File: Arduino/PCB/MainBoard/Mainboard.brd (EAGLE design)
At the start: 94.9 x 80 mm, 58 parts, among them IC1 ULN2803ADW, IC2 DS1338Z-33+, J1 FTDI_DEVICE, J2 FTDI_DEVICE, J3 DC-005, U1 ATMEGA328-AU, U4 R-78B5.0-2.0, X1 16Mhz, X2 32.768kHz

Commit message: Mainboard
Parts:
- removed U$1, U$2, U$3, U$4, U$5, U$6, U$7, U$8: GF1A-E3/67A, MainboardComponents:DO-214BA
- removed X2: 32.768kHz, IQD-Frequency-Products:HC49-3L
- added DF1, DF2, DF3, DF4, DF5, DF6, DF7, DF8: GF1A-E3/67A, MainboardComponents:DO-214BA
- added J4: XBEE CONN, SparkFun-Connectors:FTDI_DEVICE_SIDE
- added JP3: (no value), jumper:JP2
- added Q1: 32.768kHz, MainboardComponents:CRYSAL_RADIA_6.2MM
- J1: value FTDI_DEVICE -> ARDUINO PROG
- J2: value FTDI_DEVICE -> BOOTL PROG
- R1, R10, R4, R5, R6, R7, R8, R9: value 580 -> 5k3
- moved U4 3.09 mm to (7.11, 37.3)
- moved C1 2.54 mm to (68.6, 54.6)
- moved L1 2.05 mm to (11.7, 23.6)
- moved C4 2.05 mm to (14.2, 17.3), flipped to the top, turned to 0 degrees
- moved C5 2.04 mm to (14.1, 30.0), flipped to the top, turned to 0 degrees
- moved J3 1.08 mm to (9.65, 10.9)
- moved R2 0.90 mm to (60.3, 56.5)
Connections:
- new net N$41: IC2.1, Q1.P$2
- new net N$42: J4.P$5, XB1.16
- net +12V: now also DF1.C, DF2.C, DF3.C, DF4.C, DF5.C, DF6.C, DF7.C, DF8.C, IC1.10; no longer U$1.C, U$2.C, U$3.C, U$4.C, U$5.C, U$6.C, U$7.C, U$8.C
- net +3V3: now also J4.P$4
- net GND: now also J4.P$6, JP3.1, XB1.9; no longer IC1.10
- net N$13: now also J4.P$1, XB1.12; no longer IC2.1, X2.1
- net N$14: now also Q1.P$1; no longer X2.3
- net N$2: now also JP3.2
- net N$3: now also J4.P$2
- net N$35: now also J4.P$3
- net R0: now also DF8.A; no longer U$8.A
- net R1: now also DF7.A; no longer U$7.A
- net R2: now also DF6.A; no longer U$6.A
- net R3: now also DF5.A; no longer U$5.A
- net R4: now also DF4.A; no longer U$4.A
- net R5: now also DF3.A; no longer U$3.A
- net R6: now also DF2.A; no longer U$2.A
- net R7: now also DF1.A; no longer U$1.A
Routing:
- net GND: track 221.1 -> 258.6 mm
- net +3V3: track 131.4 -> 162.9 mm
- net N$35: track 38.2 -> 68.2 mm
- net N$13: track 6.39 -> 35.9 mm
- net N$2: track 48.7 -> 74.9 mm
- net N$42: track 0.00 -> 23.7 mm
- net N$3: track 38.0 -> 60.3 mm
- net N$23: track 88.9 -> 106.0 mm, vias 1 -> 0
- net N$24: track 92.5 -> 81.7 mm
- net +12V: track 157.6 -> 163.5 mm, vias 0 -> 1
- net +5V: track 65.7 -> 61.6 mm
- net N$41: track 0.00 -> 4.06 mm
- net N$7: track 13.4 -> 10.4 mm
- net N$20: track 36.2 -> 33.5 mm
- net N$6: track 13.0 -> 10.8 mm
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
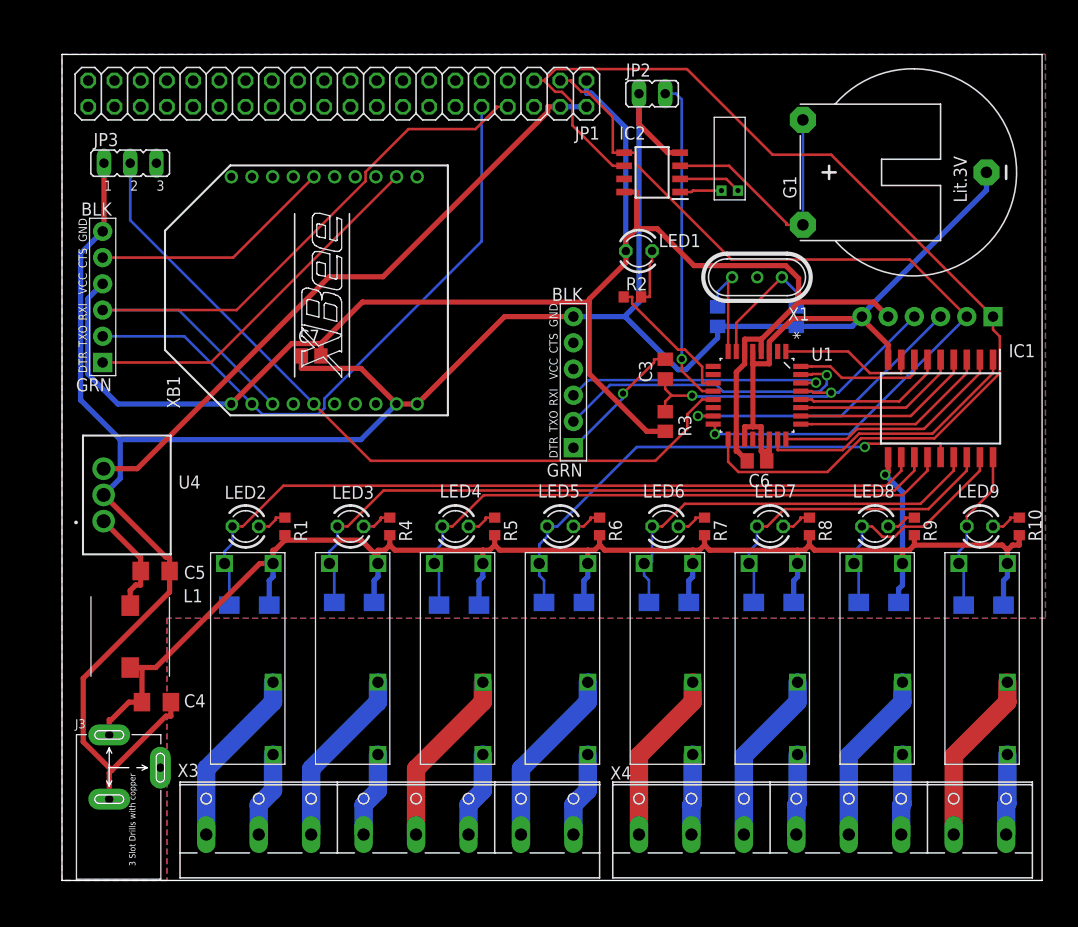
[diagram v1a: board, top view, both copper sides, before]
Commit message: 
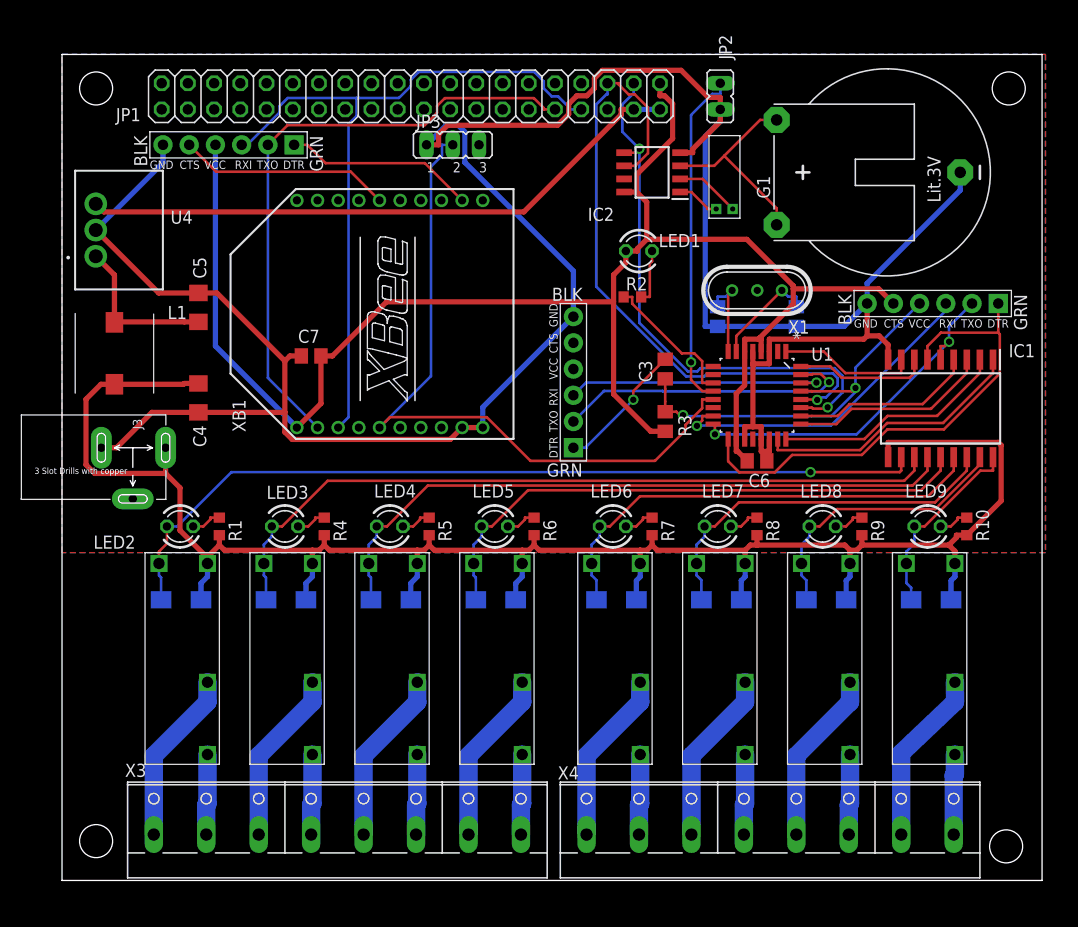
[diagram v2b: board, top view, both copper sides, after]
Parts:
- moved JP3 31.3 mm to (42.9, 71.2)
- moved J3 31.1 mm to (11.9, 41.9), turned to 0 degrees
- moved C4 29.7 mm to (18.3, 46.7), turned to 270 degrees
- moved L1 27.5 mm to (10.2, 51.1)
- moved C5 25.9 mm to (18.3, 55.5), turned to 90 degrees
- moved U4 25.7 mm to (6.35, 63.0)
- moved J4 19.1 mm to (21.2, 71.2), turned to 180 degrees
- moved JP1 7.12 mm to (38.9, 75.9)
- moved XB1 6.75 mm to (36.8, 54.9)
- moved DF1 6.62 mm to (16.8, 27.2)
- moved DF3 6.62 mm to (37.1, 27.2)
- moved JP2 6.61 mm to (68.8, 75.9), turned to 0 degrees
- moved DF2 6.61 mm to (26.9, 27.2)
- moved DF4 6.61 mm to (47.2, 27.2)
- moved LED3 6.35 mm to (26.7, 34.3)
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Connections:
- removed net N$23: IC2.6, J2.P$1, JP1.5, U1.17
- removed net N$24: IC2.5, J2.P$2, JP1.3, U1.16
- new net SCL: IC2.6, JP1.5, U1.28
- new net SDA: IC2.5, JP1.3, U1.27
- net D4: now also J2.P$2, U1.16; no longer U1.27
- net D5: now also J2.P$1, U1.17; no longer U1.28
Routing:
- net N$23: track 106.0 -> 0.00 mm
- net N$24: track 81.7 -> 0.00 mm, vias 1 -> 0
- net SCL: track 0.00 -> 64.6 mm, vias 0 -> 1
- net SDA: track 0.00 -> 54.5 mm, vias 0 -> 2
- net D5: track 14.8 -> 48.4 mm
- net +12V: track 163.5 -> 184.7 mm, vias 1 -> 0
- net D4: track 16.2 -> 34.4 mm, vias 0 -> 2
- net N$13: track 35.9 -> 18.5 mm
- net N$2: track 74.9 -> 68.7 mm
- net N$20: track 33.5 -> 39.3 mm
- net R6: track 67.9 -> 73.3 mm
- net R5: track 59.2 -> 64.4 mm
- net R7: track 77.0 -> 82.2 mm, vias 0 -> 1
- net R4: track 50.6 -> 55.5 mm, vias 1 -> 0
- net N$7: track 10.4 -> 15.3 mm
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
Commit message: 
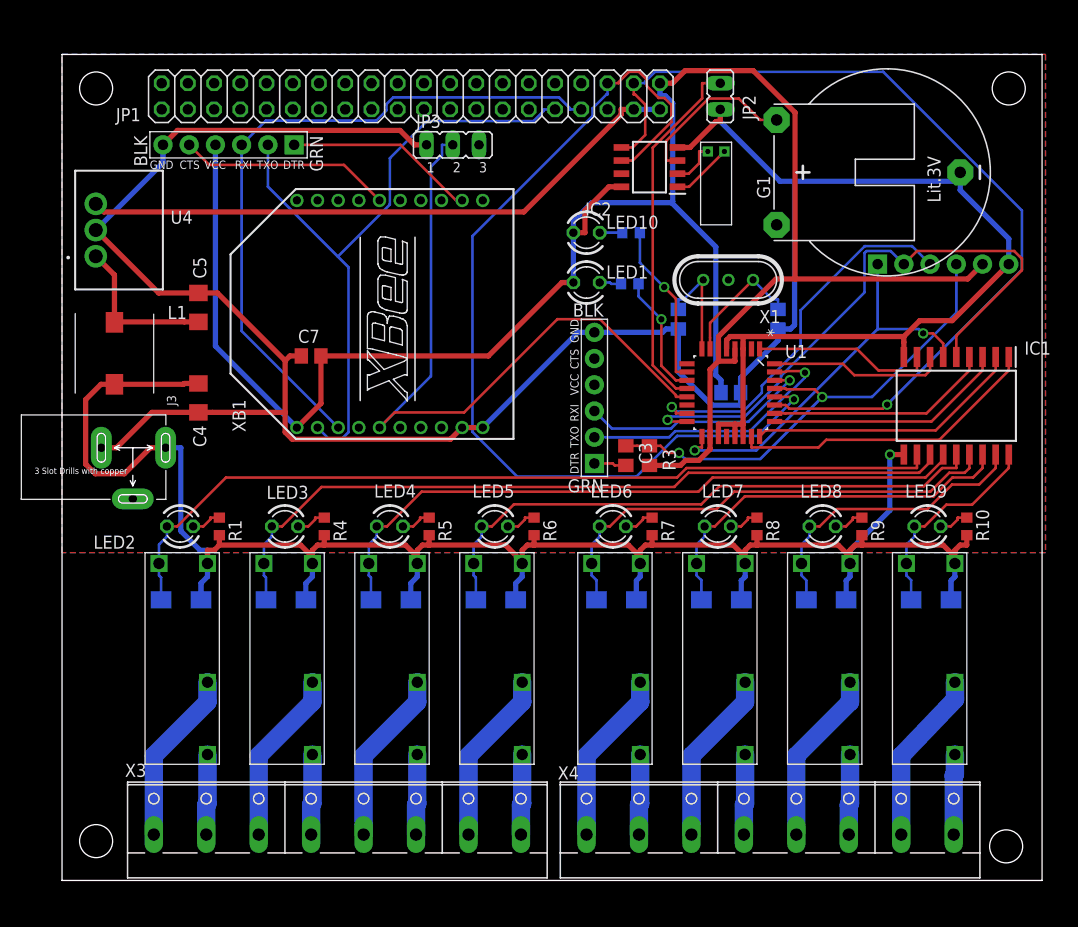
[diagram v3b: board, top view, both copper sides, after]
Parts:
- added LED10: 2mA, led:LED3MM
- added R11: 580, rcl:R0603
- moved C3 9.21 mm to (59.7, 41.1), turned to 270 degrees
- moved Q1 8.29 mm to (66.9, 71.5), turned to 0 degrees
- moved C6 7.08 mm to (69.8, 47.2), flipped to the bottom, turned to 0 degrees
- moved LED1 5.92 mm to (55.9, 57.9)
- moved J2 3.94 mm to (90.4, 59.7), flipped to the bottom
- moved C1 3.82 mm to (64.8, 54.4)
- moved R3 3.64 mm to (62.0, 41.1)
- moved X1 2.97 mm to (69.6, 58.2)
- moved U1 2.55 mm to (69.8, 47.2)
- moved J1 2.54 mm to (56.6, 46.7)
- moved C2 1.80 mm to (74.4, 54.4)
- moved IC1 1.55 mm to (91.7, 46.0)
- moved R2 1.30 mm to (60.1, 57.8), flipped to the bottom
- moved IC2 0.57 mm to (62.0, 69.1)
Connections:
- new net N$24: LED10.K, R11.2
- new net N$44: R11.1, U1.10
- net +3V3: now also LED10.A
- net N$12: no longer G1.+@1
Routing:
- net +3V3: track 159.8 -> 203.1 mm
- net SDA: track 54.5 -> 87.5 mm, vias 2 -> 1
- net SCL: track 64.6 -> 93.7 mm
- net D4: track 34.4 -> 59.0 mm, vias 2 -> 1
- net N$44: track 0.00 -> 16.0 mm, vias 0 -> 1
- net N$5: track 13.0 -> 3.13 mm, vias 1 -> 0
- net D5: track 48.4 -> 39.0 mm, vias 0 -> 2
- net N$20: track 39.3 -> 48.1 mm
- net N$22: track 31.6 -> 36.9 mm
- net N$3: track 60.0 -> 64.4 mm
- net N$35: track 71.2 -> 67.0 mm
- net D0: track 26.3 -> 30.4 mm
- net D6: track 12.9 -> 17.0 mm
- net D3: track 17.8 -> 21.9 mm
- net D2: track 19.4 -> 23.5 mm
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
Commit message: as send to allpcb
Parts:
- removed G1: CR2032, MainboardComponents:BATTERY_CR2032H
- added U$1: KEYSTONE_1066, MainboardComponents:KEYSTONE1066
- moved IC1 33.8 mm to (57.9, 44.5), flipped to the bottom
- moved JP1 29.7 mm to (68.6, 76.5)
- moved JP2 29.0 mm to (39.9, 76.5), turned to 180 degrees
- moved C1 26.9 mm to (90.2, 45.5), turned to 180 degrees
- moved X1 22.9 mm to (86.9, 43.2), turned to 90 degrees
- moved JP3 21.6 mm to (21.3, 72.0), turned to 180 degrees
- moved C2 20.9 mm to (90.2, 40.6), turned to 0 degrees
- moved J2 18.5 mm to (97.0, 42.4), turned to 90 degrees
- moved C7 14.9 mm to (22.9, 64.3), turned to 90 degrees
- moved J1 11.4 mm to (65.3, 54.1), turned to 180 degrees
- moved C3 9.71 mm to (66.3, 48.3), turned to 90 degrees
- moved U1 8.27 mm to (77.7, 44.7), turned to 180 degrees
- moved R3 7.22 mm to (63.2, 48.3), turned to 90 degrees
- moved J4 5.34 mm to (21.0, 76.6), turned to 0 degrees
- moved IC2 2.03 mm to (59.9, 69.1)
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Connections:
- net GND: now also U$1.NEG$2; no longer G1.-
- net N$12: now also U$1.POS$1; no longer G1.+
- net R0: now also DF1.A, LED2.K, REL0.A2; no longer DF8.A, LED9.K, REL7.A2
- net R1: now also DF2.A, LED3.K, REL1.A2; no longer DF7.A, LED8.K, REL6.A2
- net R2: now also DF3.A, LED4.K, REL2.A2; no longer DF6.A, LED7.K, REL5.A2
- net R3: now also DF4.A, LED5.K, REL3.A2; no longer DF5.A, LED6.K, REL4.A2
- net R4: now also DF5.A, LED6.K, REL4.A2; no longer DF4.A, LED5.K, REL3.A2
- net R5: now also DF6.A, LED7.K, REL5.A2; no longer DF3.A, LED4.K, REL2.A2
- net R6: now also DF7.A, LED8.K, REL6.A2; no longer DF2.A, LED3.K, REL1.A2
- net R7: now also DF8.A, LED9.K, REL7.A2; no longer DF1.A, LED2.K, REL0.A2
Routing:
- net R7: track 83.8 -> 36.5 mm
- net R6: track 74.6 -> 27.6 mm
- net R5: track 65.6 -> 18.7 mm
- net R4: track 57.1 -> 13.4 mm
- net R0: track 20.4 -> 54.6 mm
- net SCL: track 93.7 -> 126.0 mm, vias 1 -> 0
- net +3V3: track 203.1 -> 170.9 mm, vias 0 -> 1
- net N$13: track 18.5 -> 50.6 mm
- net +5V: track 59.4 -> 88.7 mm, vias 0 -> 1
- net R3: track 47.1 -> 21.5 mm
- net D5: track 39.0 -> 62.9 mm, vias 2 -> 1
- net +12V: track 181.1 -> 159.4 mm
- net SDA: track 87.5 -> 109.1 mm, vias 1 -> 0
- net N$35: track 67.0 -> 86.4 mm
- net N$3: track 64.4 -> 82.0 mm, vias 0 -> 1
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
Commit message: ready to send v2
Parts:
- moved JP2 5.59 mm to (34.3, 76.5)
- moved C7 1.78 mm to (22.9, 62.5)
- moved XB1 1.52 mm to (37.6, 54.6)
- moved Q1 1.27 mm to (66.2, 71.0)
- moved U$1 1.00 mm to (87.6, 60.2)
- moved C1 0.76 mm to (90.2, 44.7)
- moved IC2 0.76 mm to (59.9, 68.3)
- moved X1 0.73 mm to (86.9, 42.4)
- moved C2 0.51 mm to (90.2, 40.1)
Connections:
- net GND: now also JP1.14, JP1.20, JP1.6, JP1.9
- net N$15: now also X3.2; no longer X3.1
- net N$16: now also X3.3; no longer X3.4
- net N$17: now also X3.4; no longer X3.3
- net N$18: now also X3.5; no longer X3.6
- net N$19: now also X3.6; no longer X3.5
- net N$21: now also X3.7; no longer X3.8
- net N$23: now also X4.7; no longer X4.8
- net N$25: now also X3.8; no longer X3.7
- net N$26: now also X4.1; no longer X4.2
- net N$27: now also X4.2; no longer X4.1
- net N$28: now also X4.3; no longer X4.4
- net N$29: now also X4.4; no longer X4.3
- net N$30: now also X4.5; no longer X4.6
- net N$31: now also X4.6; no longer X4.5
- net N$33: now also X4.8; no longer X4.7
- net N$4: now also X3.1; no longer X3.2
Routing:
- net GND: track 245.4 -> 285.4 mm, vias 2 -> 0
- net +12V: track 159.4 -> 180.8 mm, vias 1 -> 0
- net SCL: track 126.0 -> 107.4 mm, vias 0 -> 2
- net +3V3: track 170.9 -> 154.8 mm, vias 1 -> 0
- net SDA: track 109.1 -> 94.1 mm, vias 0 -> 2
- net D4: track 67.7 -> 81.7 mm, vias 2 -> 1
- net +5V: track 88.7 -> 99.8 mm
- net N$3: track 82.0 -> 92.6 mm
- net N$22: track 26.8 -> 35.6 mm
- net R7: track 36.5 -> 44.0 mm
- net N$10: track 21.4 -> 28.4 mm
- net N$41: track 13.7 -> 7.33 mm
- net N$34: track 51.1 -> 56.3 mm, vias 0 -> 1
- net N$14: track 9.61 -> 5.28 mm
- net N$12: track 15.0 -> 19.0 mm
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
